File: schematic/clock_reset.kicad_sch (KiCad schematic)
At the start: 10 parts, among them U22 74LS04, U7 74LS05

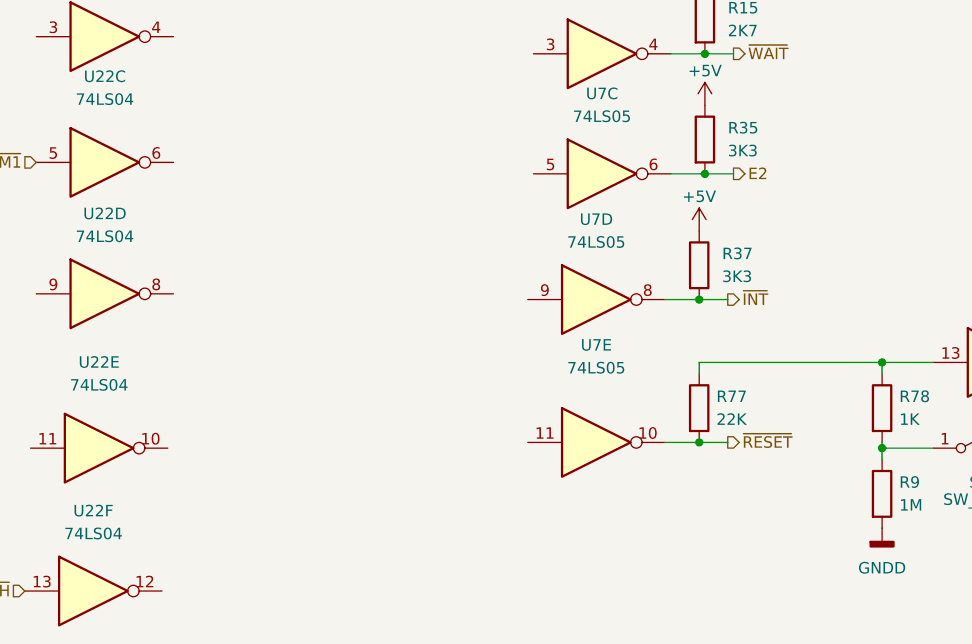
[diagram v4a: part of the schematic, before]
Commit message: added u5 decoder lines, need to rename for chip selects that they actually are in future.
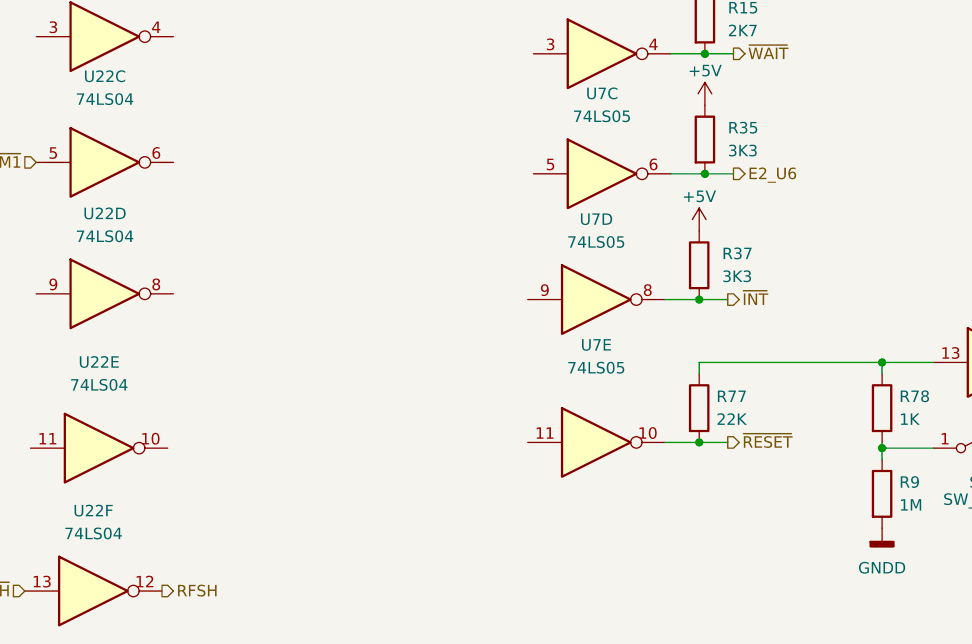
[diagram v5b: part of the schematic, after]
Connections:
- net RFSH: now reaches U22.12
- net E2 renamed E2_U6
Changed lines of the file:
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@@
     (stroke (width 0) (type default) (color 0 0 0 0))
   )
-  (hierarchical_label "E2" (shape output) (at 186.055 114.935 0)
+  (hierarchical_label "E2_U6" (shape output) (at 186.055 114.935 0)
     (effects (font (size 1.27 1.27)) (justify left))
   )
@@
     (effects (font (size 1.27 1.27)) (justify right))
   )
+  (hierarchical_label "RFSH" (shape output) (at 122.555 161.29 0)
+    (effects (font (size 1.27 1.27)) (justify left))
+  )
   (hierarchical_label "~{M1}" (shape input) (at 108.585 113.665 180)

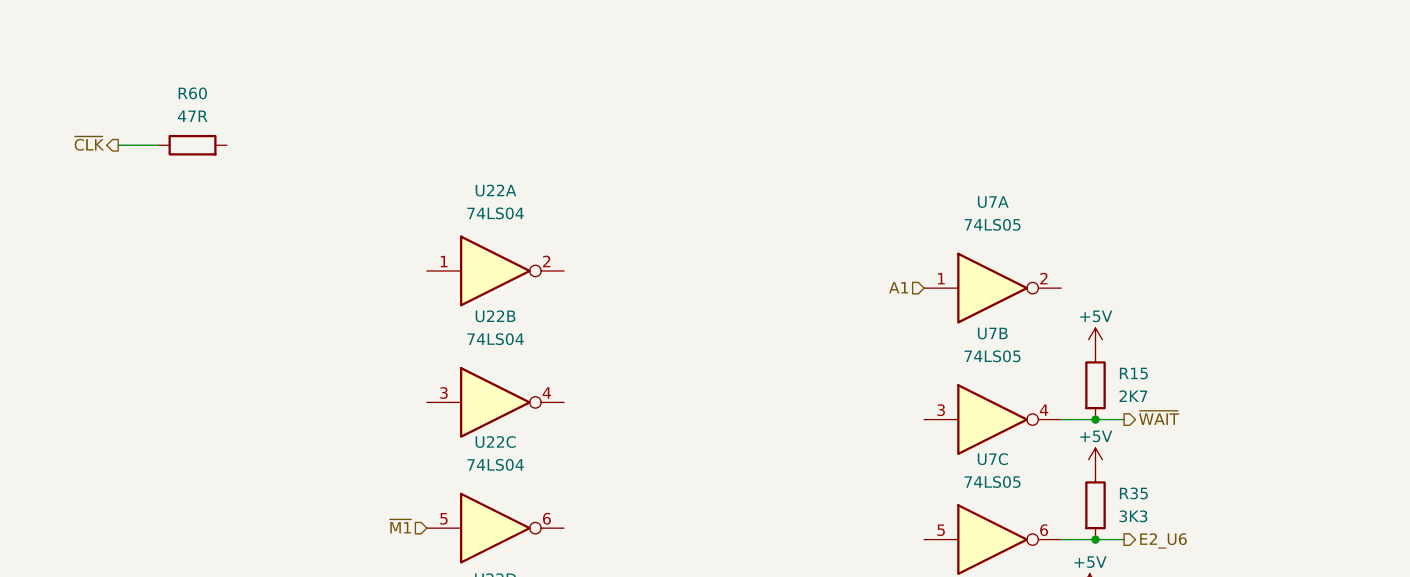
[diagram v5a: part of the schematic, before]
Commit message: completed sound block, finished cart io port, and finished decoder.
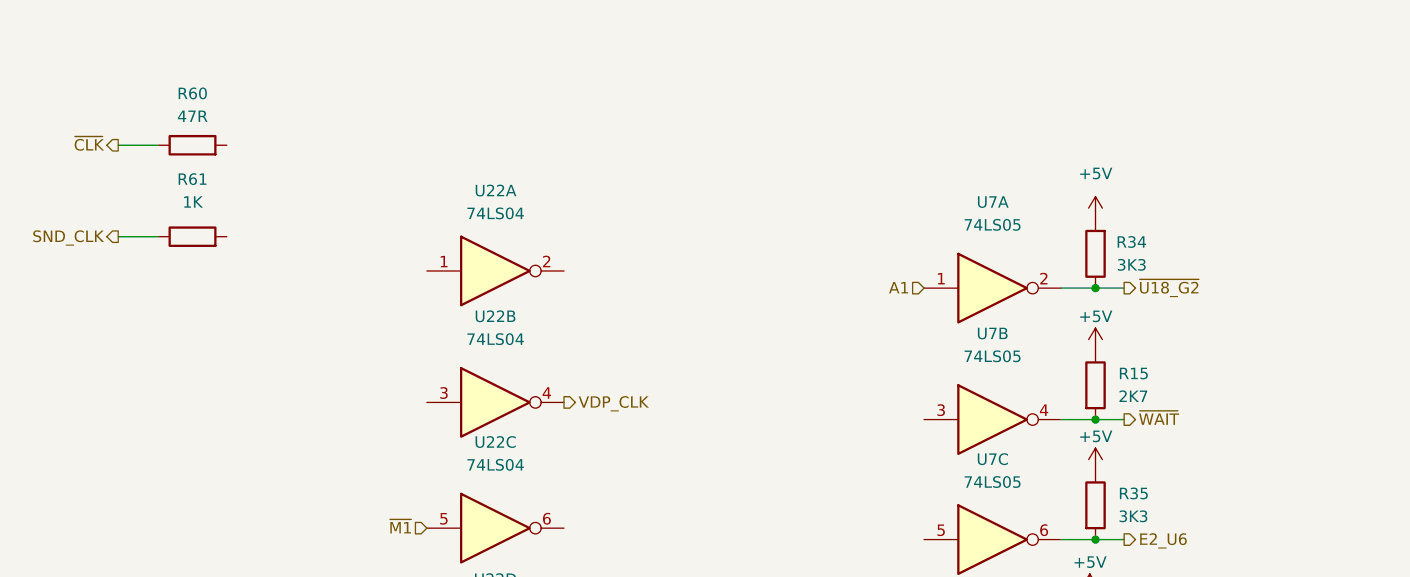
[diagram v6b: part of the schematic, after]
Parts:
- added R34: 3K3, symbol Device:R
- added R61: 1K, symbol Device:R
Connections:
- net +5V: now also R34.2
- net ~{U18_G2}: now reaches U7.2
- net ~{U18_G2}: now also R34.1
- net VDP_CLK: now reaches U22.4
- new net SND_CLK: R61.1
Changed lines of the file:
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@@
   (junction (at 202.565 145.415) (diameter 0) (color 0 0 0 0)
   )
+  (junction (at 182.88 86.995) (diameter 0) (color 0 0 0 0)
+  )
   (junction (at 202.565 135.89) (diameter 0) (color 0 0 0 0)
   )
@@
   (junction (at 182.88 114.935) (diameter 0) (color 0 0 0 0)
   )
+  (wire (pts (xy 74.295 81.28) (xy 78.74 81.28))
+    (stroke (width 0) (type default) (color 0 0 0 0))
+  )
   (wire (pts (xy 182.245 144.78) (xy 185.42 144.78))
     (stroke (width 0) (type default) (color 0 0 0 0))
   )
+  (wire (pts (xy 182.88 86.995) (xy 179.07 86.995))
+    (stroke (width 0) (type default) (color 0 0 0 0))
+  )
   (wire (pts (xy 202.565 135.89) (xy 202.565 137.16))
     (stroke (width 0) (type default) (color 0 0 0 0))
@@
   )
   (wire (pts (xy 178.435 128.905) (xy 182.245 128.905))
+    (stroke (width 0) (type default) (color 0 0 0 0))
+  )
+  (wire (pts (xy 186.055 86.995) (xy 182.88 86.995))
     (stroke (width 0) (type default) (color 0 0 0 0))
   )
@@
     (effects (font (size 1.27 1.27)) (justify right))
   )
+  (hierarchical_label "VDP_CLK" (shape output) (at 123.825 99.695 0)
+    (effects (font (size 1.27 1.27)) (justify left))
+  )
+  (hierarchical_label "SND_CLK" (shape output) (at 74.295 81.28 180)
+    (effects (font (size 1.27 1.27)) (justify right))
+  )
   (hierarchical_label "A1" (shape input) (at 163.83 86.995 180)
     (effects (font (size 1.27 1.27)) (justify right))
@@
   (hierarchical_label "~{RESET}" (shape output) (at 185.42 144.78 0)
     (effects (font (size 1.27 1.27)) (justify left))
+  )
+  (hierarchical_label "~{U18_G2}" (shape output) (at 186.055 86.995 0)
+    (effects (font (size 1.27 1.27)) (justify left))
+  )
+  (symbol (lib_id "power:+5V") (at 182.88 79.375 0) (unit 1)
+    (in_bom yes) (on_board yes) (fields_autoplaced)
+    (property "Reference" "#PWR?" (id 0) (at 182.88 83.185 0)
+      (effects (font (size 1.27 1.27)) hide)
+    )
+    (property "Value" "+5V" (id 1) (at 182.88 74.295 0))
+    (property "Footprint" "" (id 2) (at 182.88 79.375 0)
+      (effects (font (size 1.27 1.27)) hide)
+    )
+    (property "Datasheet" "" (id 3) (at 182.88 79.375 0)
+      (effects (font (size 1.27 1.27)) hide)
+    )
+    (pin "1")
   )
   (symbol (lib_id "power:GNDD") (at 202.565 154.305 0) (unit 1)
@@
     (pin "7")
   )
+  (symbol (lib_id "Device:R") (at 82.55 81.28 90) (unit 1)
+    (in_bom yes) (on_board yes) (fields_autoplaced)
+    (property "Reference" "R61" (id 0) (at 82.55 74.93 90))
+    (property "Value" "1K" (id 1) (at 82.55 77.47 90))
+    (property "Footprint" "" (id 2) (at 82.55 83.058 90)
+      (effects (font (size 1.27 1.27)) hide)
+    )
+    (property "Datasheet" "~" (id 3) (at 82.55 81.28 0)
+      (effects (font (size 1.27 1.27)) hide)
+    )
+    (pin "1")
+    (pin "2")
+  )
   (symbol (lib_id "Device:R") (at 182.245 125.095 0) (unit 1)
     (in_bom yes) (on_board yes)
@@
     (pin "7")
   )
+  (symbol (lib_id "Device:R") (at 182.88 83.185 180) (unit 1)
+    (in_bom yes) (on_board yes)
+    (property "Reference" "R34" (id 0) (at 188.595 81.915 0)
+      (effects (font (size 1.27 1.27)) (justify left))
+    )
+    (property "Value" "3K3" (id 1) (at 188.595 84.455 0)
+      (effects (font (size 1.27 1.27)) (justify left))
+    )
+    (property "Footprint" "" (id 2) (at 184.658 83.185 90)
+      (effects (font (size 1.27 1.27)) hide)
+    )
+    (property "Datasheet" "~" (id 3) (at 182.88 83.185 0)
+      (effects (font (size 1.27 1.27)) hide)
+    )
+    (pin "1")
+    (pin "2")
+  )
   (symbol (lib_id "74xx:74LS04") (at 116.205 128.27 0) (unit 4)

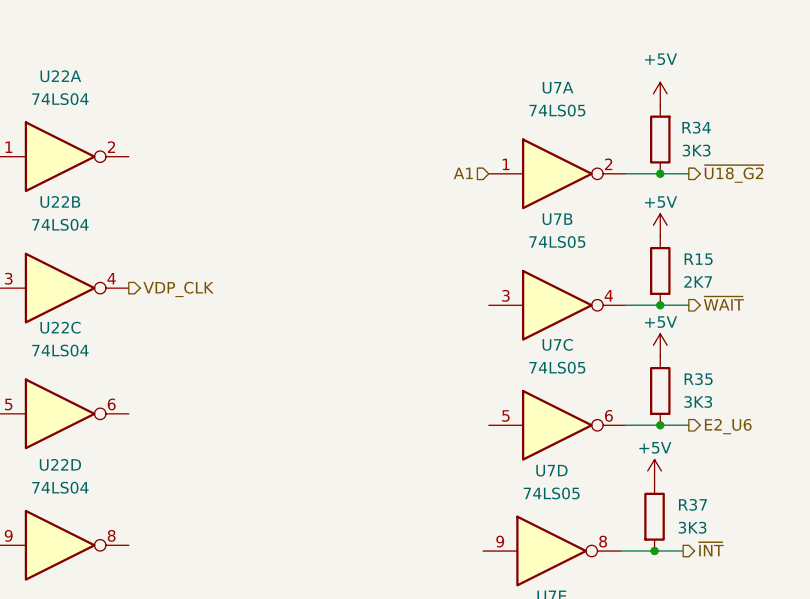
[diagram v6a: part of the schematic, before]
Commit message: fixed some more line names, added a expansion port io pin.
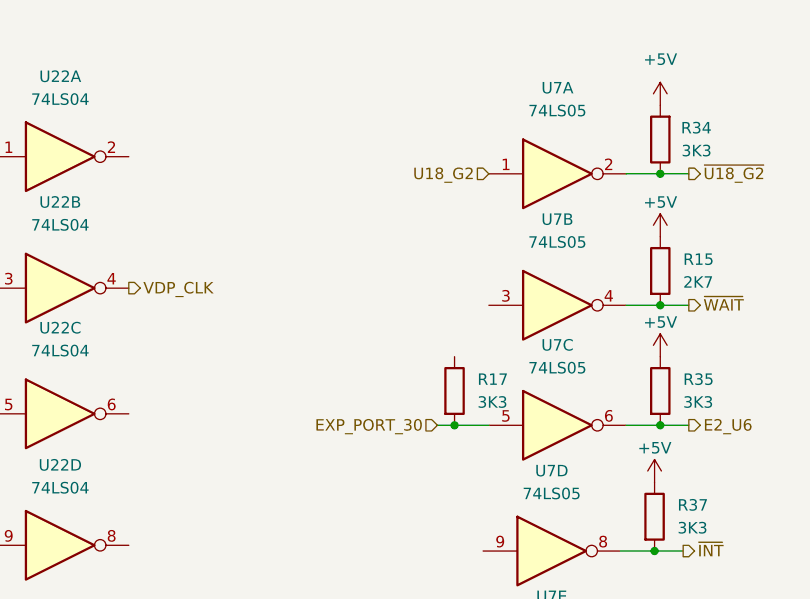
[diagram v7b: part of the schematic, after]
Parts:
- added R17: 3K3, symbol Device:R
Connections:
- net EXP_PORT_30: now reaches U7.5
- net EXP_PORT_30: now also R17.2
- net A1 renamed U18_G2
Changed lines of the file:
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@@
 (kicad_sch (version 20211123) (generator eeschema)
   (paper "A4")
+  (junction (at 160.02 114.935) (diameter 0) (color 0 0 0 0)
+  )
   (junction (at 182.245 128.905) (diameter 0) (color 0 0 0 0)
   )
@@
     (stroke (width 0) (type default) (color 0 0 0 0))
   )
+  (wire (pts (xy 158.115 114.935) (xy 160.02 114.935))
+    (stroke (width 0) (type default) (color 0 0 0 0))
+  )
   (wire (pts (xy 202.565 144.78) (xy 202.565 145.415))
     (stroke (width 0) (type default) (color 0 0 0 0))
@@
     (stroke (width 0) (type default) (color 0 0 0 0))
   )
+  (wire (pts (xy 160.02 114.935) (xy 163.83 114.935))
+    (stroke (width 0) (type default) (color 0 0 0 0))
+  )
   (hierarchical_label "E2_U6" (shape output) (at 186.055 114.935 0)
     (effects (font (size 1.27 1.27)) (justify left))
@@
     (effects (font (size 1.27 1.27)) (justify right))
   )
-  (hierarchical_label "A1" (shape input) (at 163.83 86.995 180)
+  (hierarchical_label "U18_G2" (shape input) (at 163.83 86.995 180)
     (effects (font (size 1.27 1.27)) (justify right))
   )
@@
   (hierarchical_label "~{INT}" (shape output) (at 185.42 128.905 0)
     (effects (font (size 1.27 1.27)) (justify left))
+  )
+  (hierarchical_label "EXP_PORT_30" (shape input) (at 158.115 114.935 180)
+    (effects (font (size 1.27 1.27)) (justify right))
   )
   (hierarchical_label "~{WAIT}" (shape output) (at 186.055 101.6 0)
@@
     (pin "1")
   )
+  (symbol (lib_id "Device:R") (at 160.02 111.125 0) (unit 1)
+    (in_bom yes) (on_board yes) (fields_autoplaced)
+    (property "Reference" "R17" (id 0) (at 162.56 109.8549 0)
+      (effects (font (size 1.27 1.27)) (justify left))
+    )
+    (property "Value" "3K3" (id 1) (at 162.56 112.3949 0)
+      (effects (font (size 1.27 1.27)) (justify left))
+    )
+    (property "Footprint" "" (id 2) (at 158.242 111.125 90)
+      (effects (font (size 1.27 1.27)) hide)
+    )
+    (property "Datasheet" "~" (id 3) (at 160.02 111.125 0)
+      (effects (font (size 1.27 1.27)) hide)
+    )
+    (pin "1")
+    (pin "2")
+  )
   (symbol (lib_id "74xx:74LS05") (at 171.45 101.6 0) (unit 2)
